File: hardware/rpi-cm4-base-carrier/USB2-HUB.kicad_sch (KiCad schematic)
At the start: 33 parts, among them J10 Conn_02x05_Odd_Even, J11 XM7B-0442, J9 690-008-221-904, U5 FSUSB42MUX, U6 USB2514B-I/M2, U8 AP22653W6, Y1 CX3225CA24000D0HSSCC

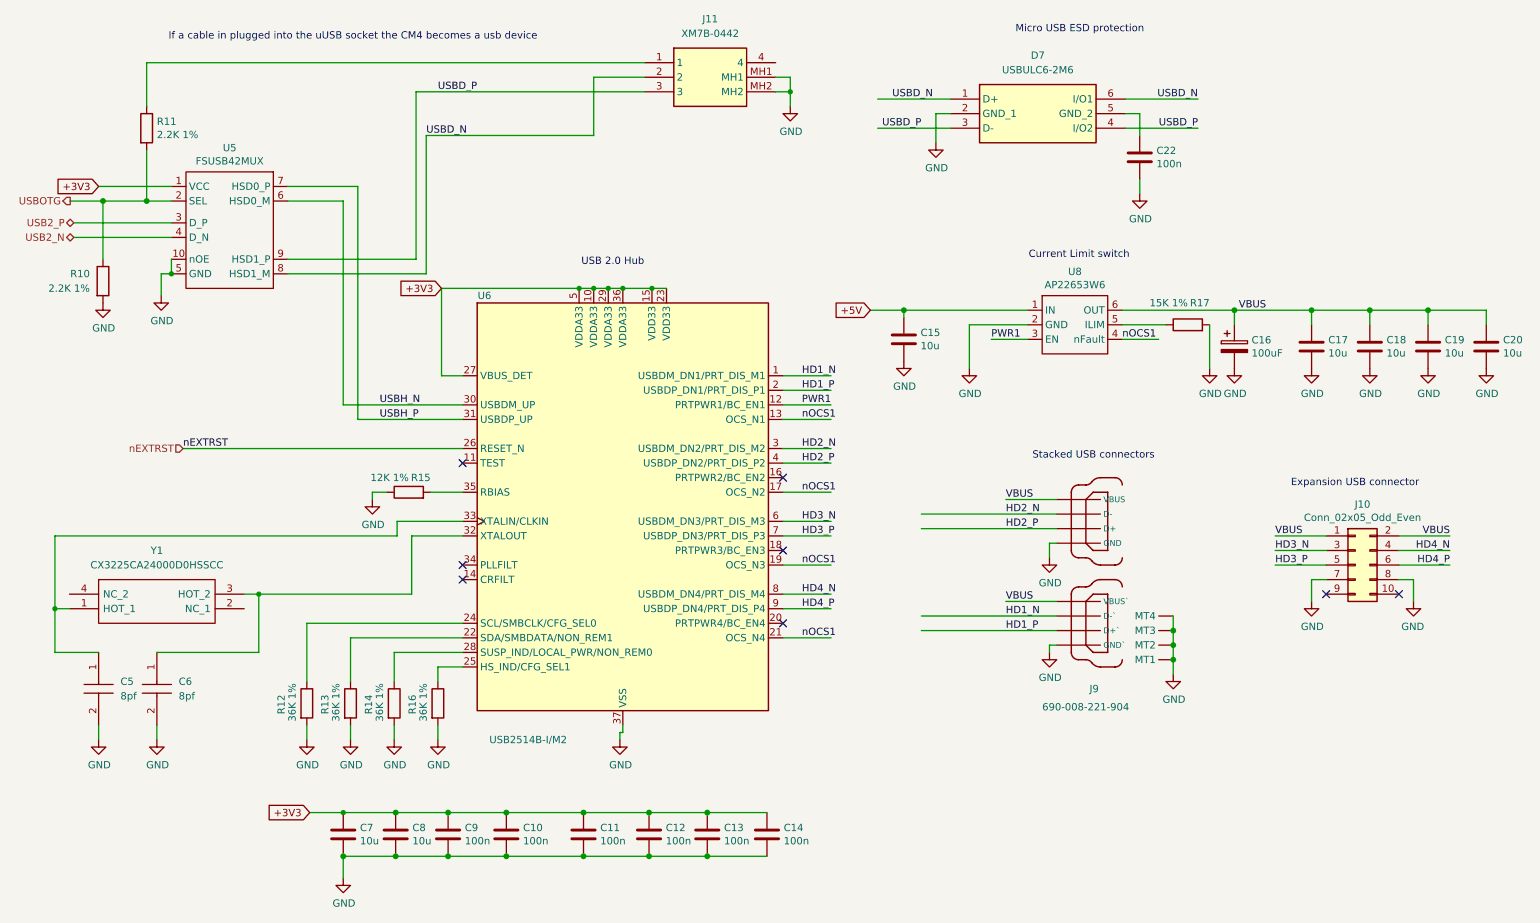
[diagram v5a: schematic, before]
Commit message: convert IC refs to U refs and re-annotate, add fiducials and extra via stitching to layout
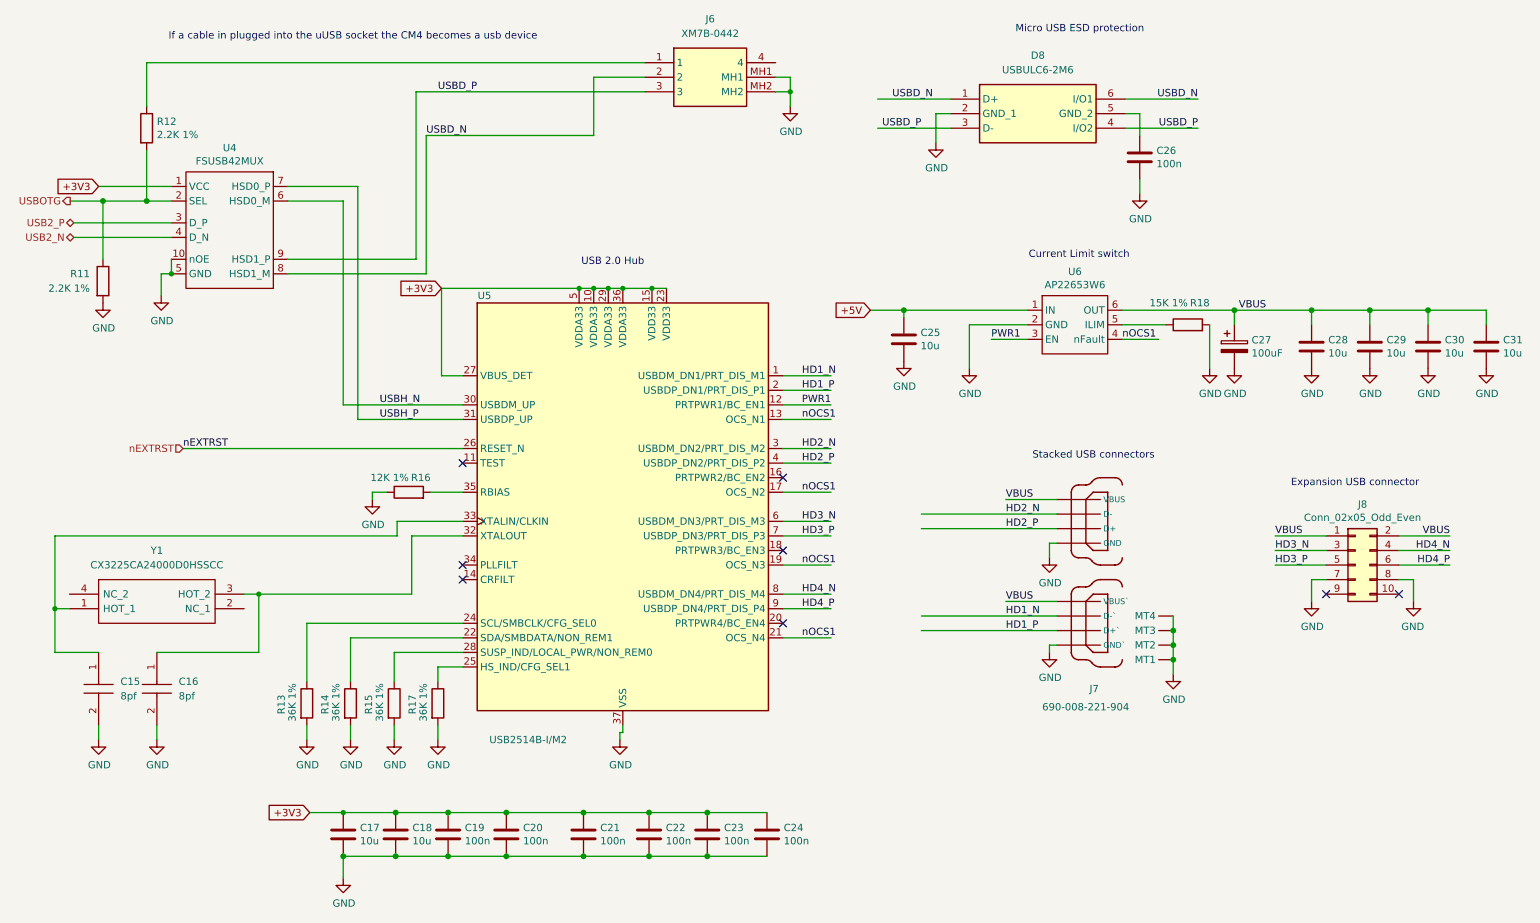
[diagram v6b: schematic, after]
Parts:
- renumbered C5 to C15, C6 to C16, C7 to C17, C8 to C18, C9 to C19, C10 to C20, C11 to C21, C12 to C22, C13 to C23, C14 to C24, C15 to C25, C22 to C26, C16 to C27, C17 to C28, C18 to C29, C19 to C30, C20 to C31, D7 to D8, J11 to J6, J9 to J7, J10 to J8, R10 to R11, R11 to R12, R12 to R13, R13 to R14, R14 to R15, R15 to R16, R16 to R17, R17 to R18, U5 to U4, U6 to U5, U8 to U6

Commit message: design files exported ready for manufacture, LCSC part numbers added throughout the library
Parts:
- C15, C16: LCSC Part # (none) -> C5858296; LCSC Part Number (none) -> C5858296
- C17, C18, C25, C28, C29, C30, C31: LCSC Part # (none) -> C326595; LCSC Part Number (none) -> C326595
- C19, C20, C21, C22, C23, C24, C26: LCSC Part # (none) -> C152724; LCSC Part Number (none) -> C152724
- C27: LCSC Part # (none) -> C600591; LCSC Part Number (none) -> C600591
- D8: LCSC Part # (none) -> C672213; LCSC Part Number (none) -> C672213
- J6: LCSC Part # (none) -> C114097; LCSC Part Number (none) -> C114097
- J7: LCSC Part # (none) -> C456021; LCSC Part Number (none) -> C456021
- J8: LCSC Part # (none) -> C492422; LCSC Part Number (none) -> C492422
- R11, R12: LCSC Part # (none) -> C186333; LCSC Part Number (none) -> C186333
- R13, R14, R15, R17: LCSC Part # (none) -> C131573; LCSC Part Number (none) -> C131573
- R16: LCSC Part # (none) -> C186350; LCSC Part Number (none) -> C186350
- R18: LCSC Part # (none) -> C2576181; LCSC Part Number (none) -> C2576181
- U4: LCSC Part # (none) -> C11355; LCSC Part Number (none) -> C11355
- U5: LCSC Part # (none) -> C220679; LCSC Part Number (none) -> C220679
- U6: LCSC Part # (none) -> C2158037; LCSC Part Number (none) -> C2158037
- Y1: LCSC Part # (none) -> C6580408; LCSC Part Number (none) -> C6580408
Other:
- title: (none) -> Raspberry Pi Compute Module 4 Control Node
